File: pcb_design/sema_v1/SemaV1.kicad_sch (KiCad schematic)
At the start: 8 parts, among them IC1 PIC24FJ64GA002-I_SP

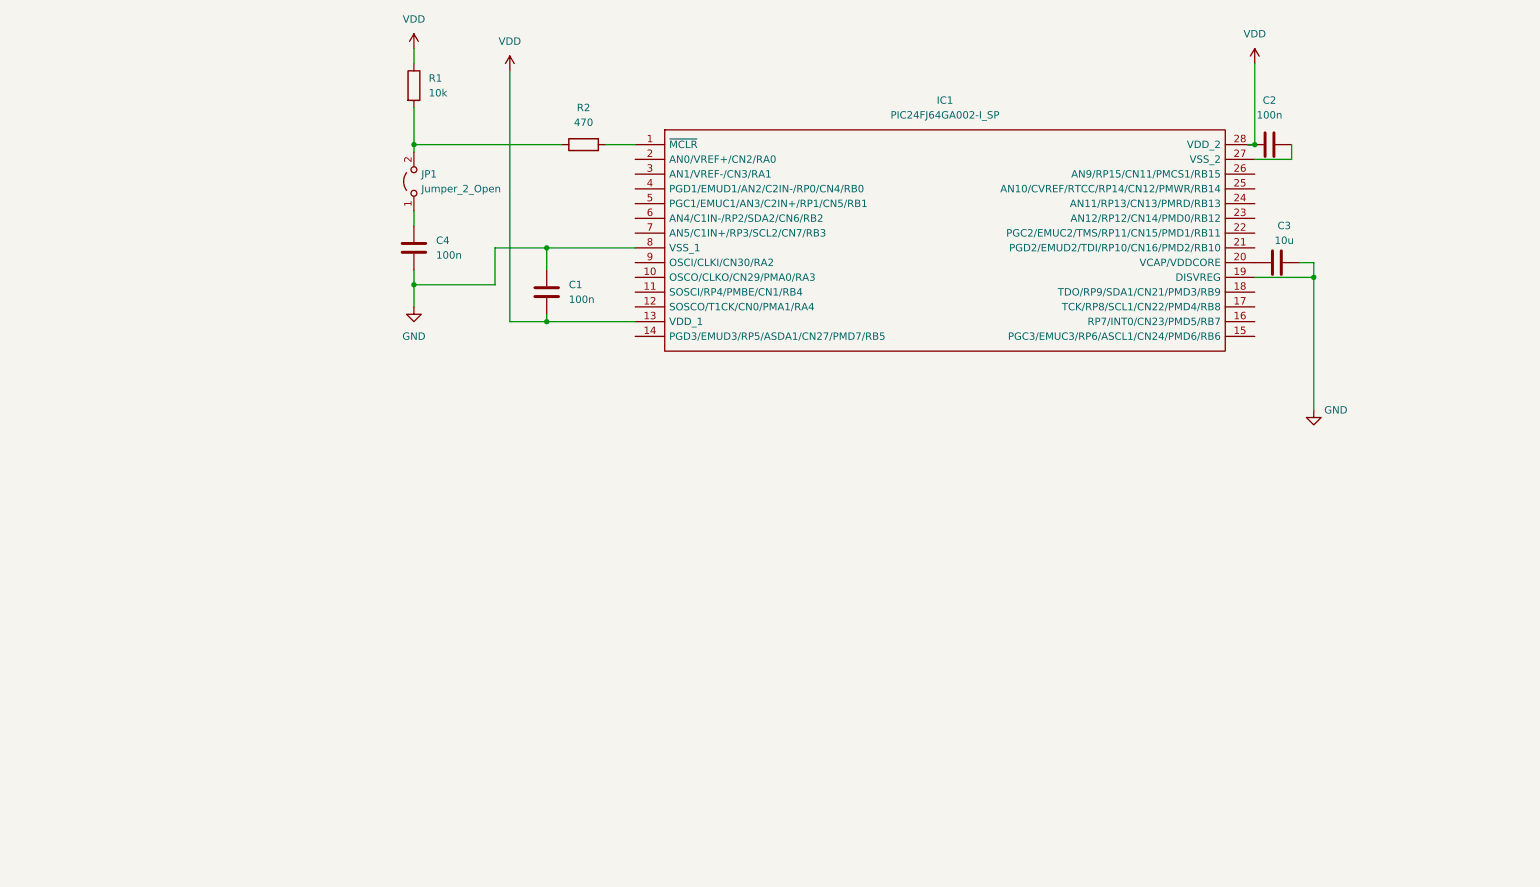
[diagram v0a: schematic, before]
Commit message: - Azuriranje seme
- Dodavanje modula za WiFi
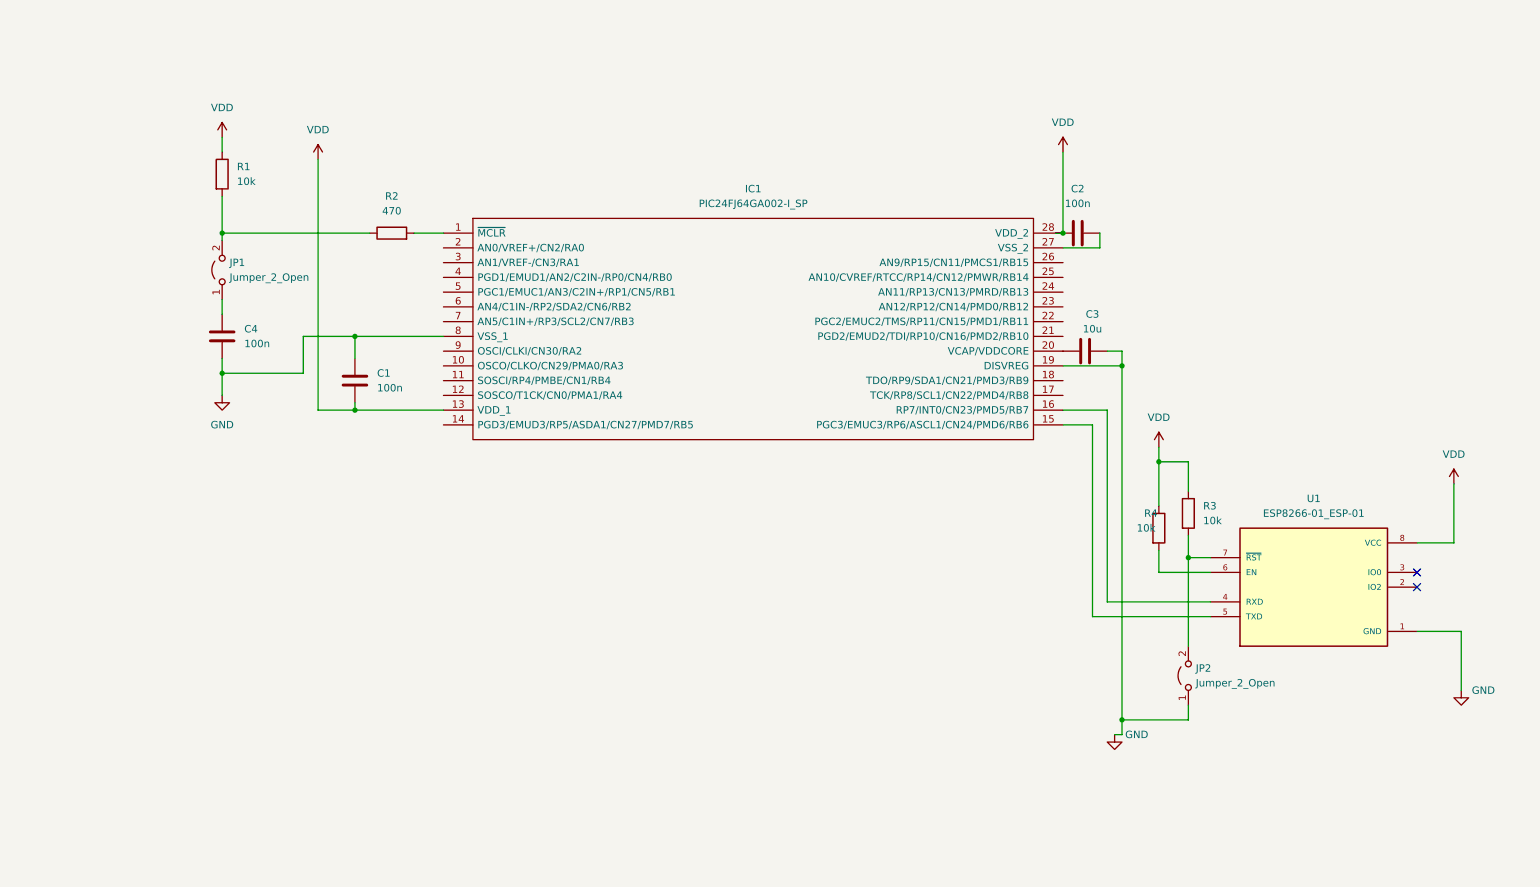
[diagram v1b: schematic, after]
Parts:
- added JP2: Jumper_2_Open, symbol Jumper:Jumper_2_Open
- added R3, R4: 10k, symbol Device:R
- added U1: ESP8266-01_ESP-01, ESP8266-01_ESP-01:XCVR_ESP8266-01_ESP-01, symbol ESP8266-01_ESP-01:ESP8266-01_ESP-01
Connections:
- net GND: now also JP2.1 (A), U1.1 (GND)
- net VDD: now also R3.1, R4.1, U1.8 (VCC)
- net at IC1.15 (PGC3/EMUC3/RP6/ASCL1/CN24/PMD6/RB6): now also U1.5 (TXD)
- net at IC1.16 (RP7/INT0/CN23/PMD5/RB7): now also U1.4 (RXD)
- new net: R4.2, U1.6 (EN)
- new net: JP2.2 (B), R3.2, U1.7 (~{RST})
- no-connect marks 0 -> 2
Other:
- moved on the sheet: C1, C2, C3, C4, IC1, JP1, R1, R2

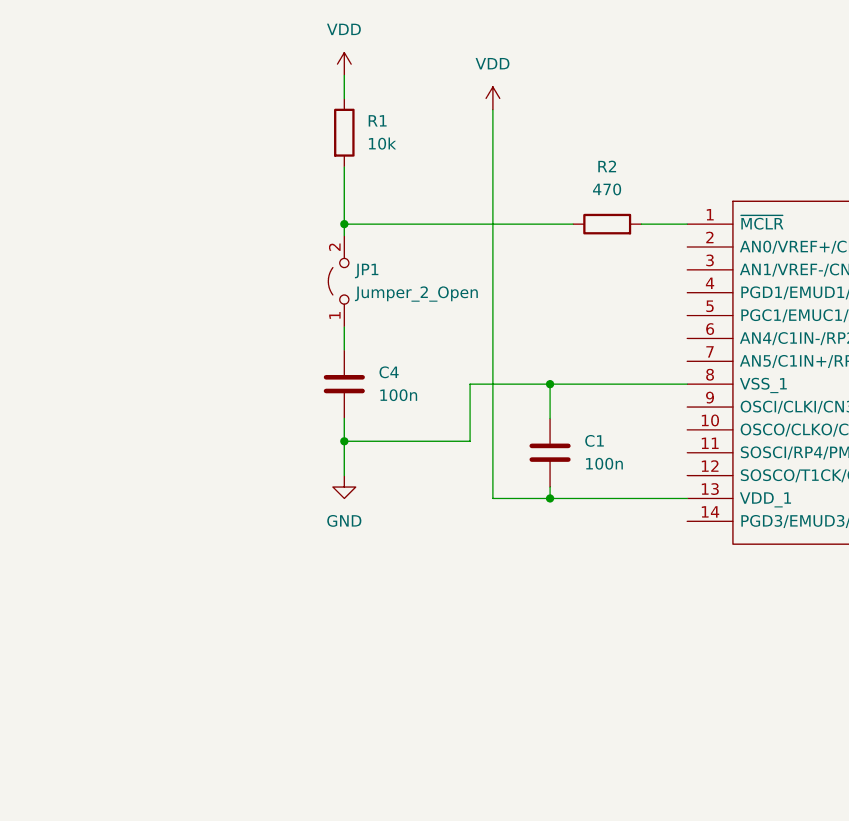
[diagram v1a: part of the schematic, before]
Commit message: -Dodavanje bloka za programiranje na šemu
  - Podrazumijeva dodavanje konektora za pinove i spajanja sa mikrokontrolerom
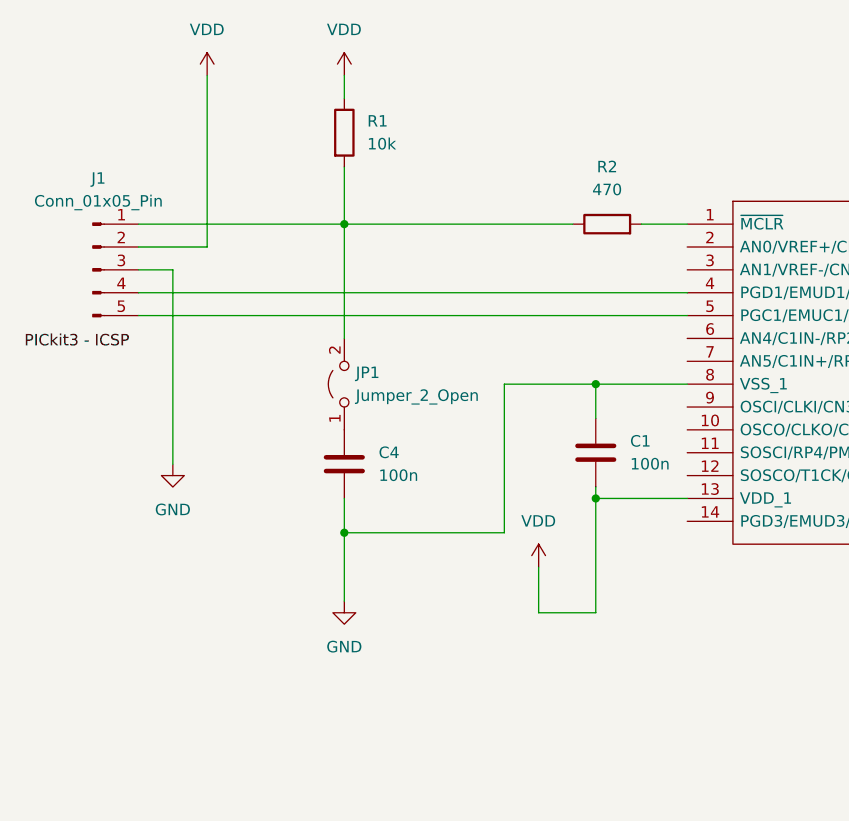
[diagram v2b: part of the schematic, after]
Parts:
- added J1: Conn_01x05_Pin, symbol Connector:Conn_01x05_Pin
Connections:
- net GND: now also J1.3 (Pin_3)
- net VDD: now also J1.2 (Pin_2)
- net at JP1.2 (B), R1.2, R2.1: now also J1.1 (Pin_1)
- net at IC1.4 (PGD1/EMUD1/AN2/C2IN-/RP0/CN4/RB0): now also J1.4 (Pin_4)
- net at IC1.5 (PGC1/EMUC1/AN3/C2IN+/RP1/CN5/RB1): now also J1.5 (Pin_5)
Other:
- moved on the sheet: C1, C4, JP1

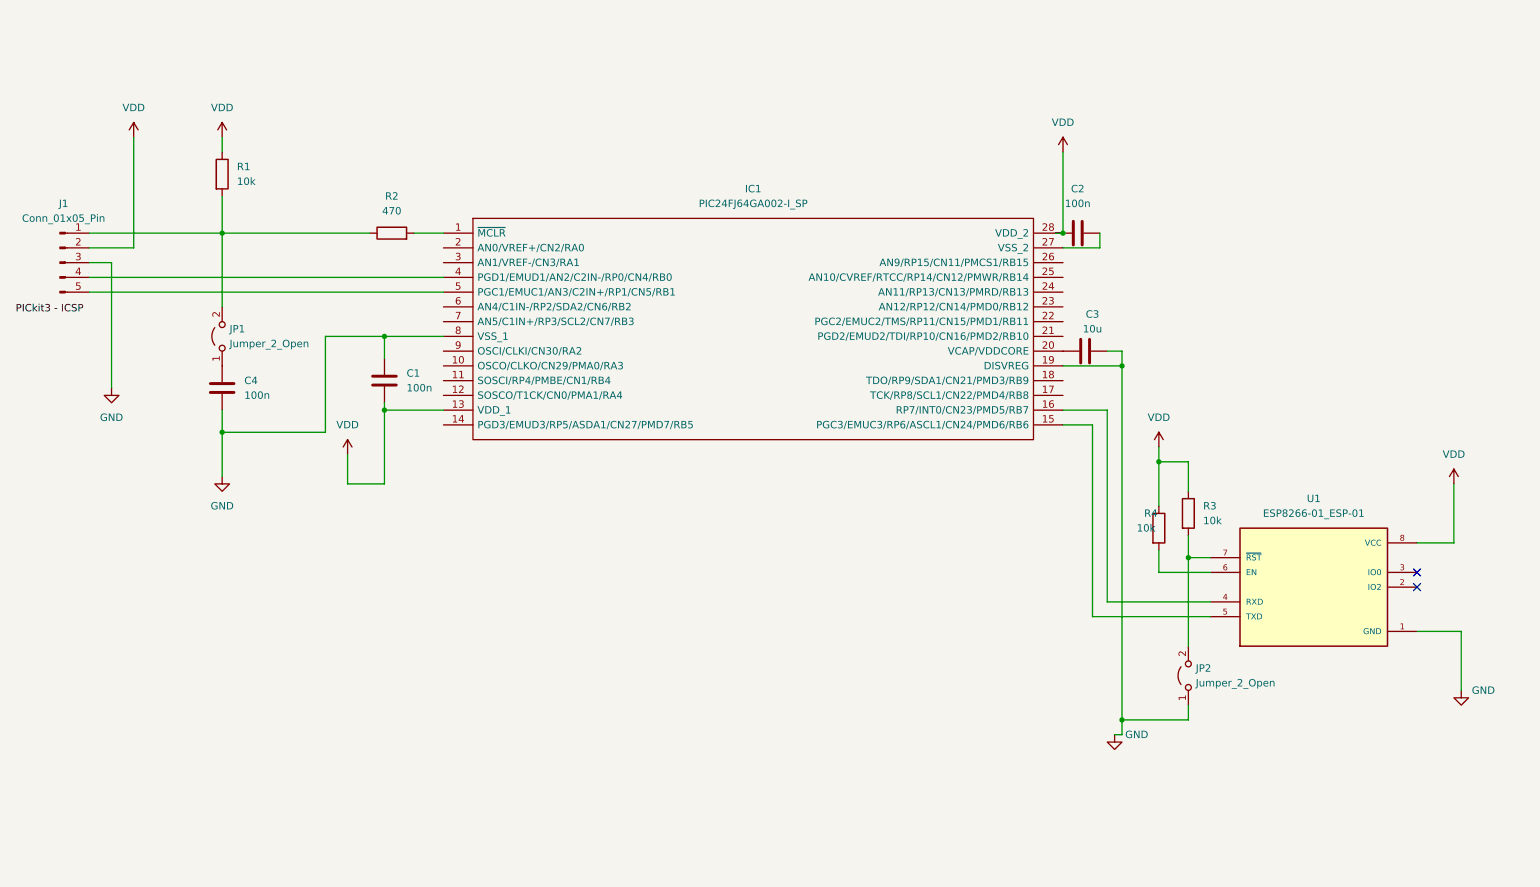
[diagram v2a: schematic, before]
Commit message: Azuriranje seme
 - Dodavanje edge connector-a na semu, spajanje I2C pinova sa mikrokontrolera i spajanje napajanja i mase

 - Dodavanje ostalih konektora za eksterne interfejse (I2C, UART, SPI)
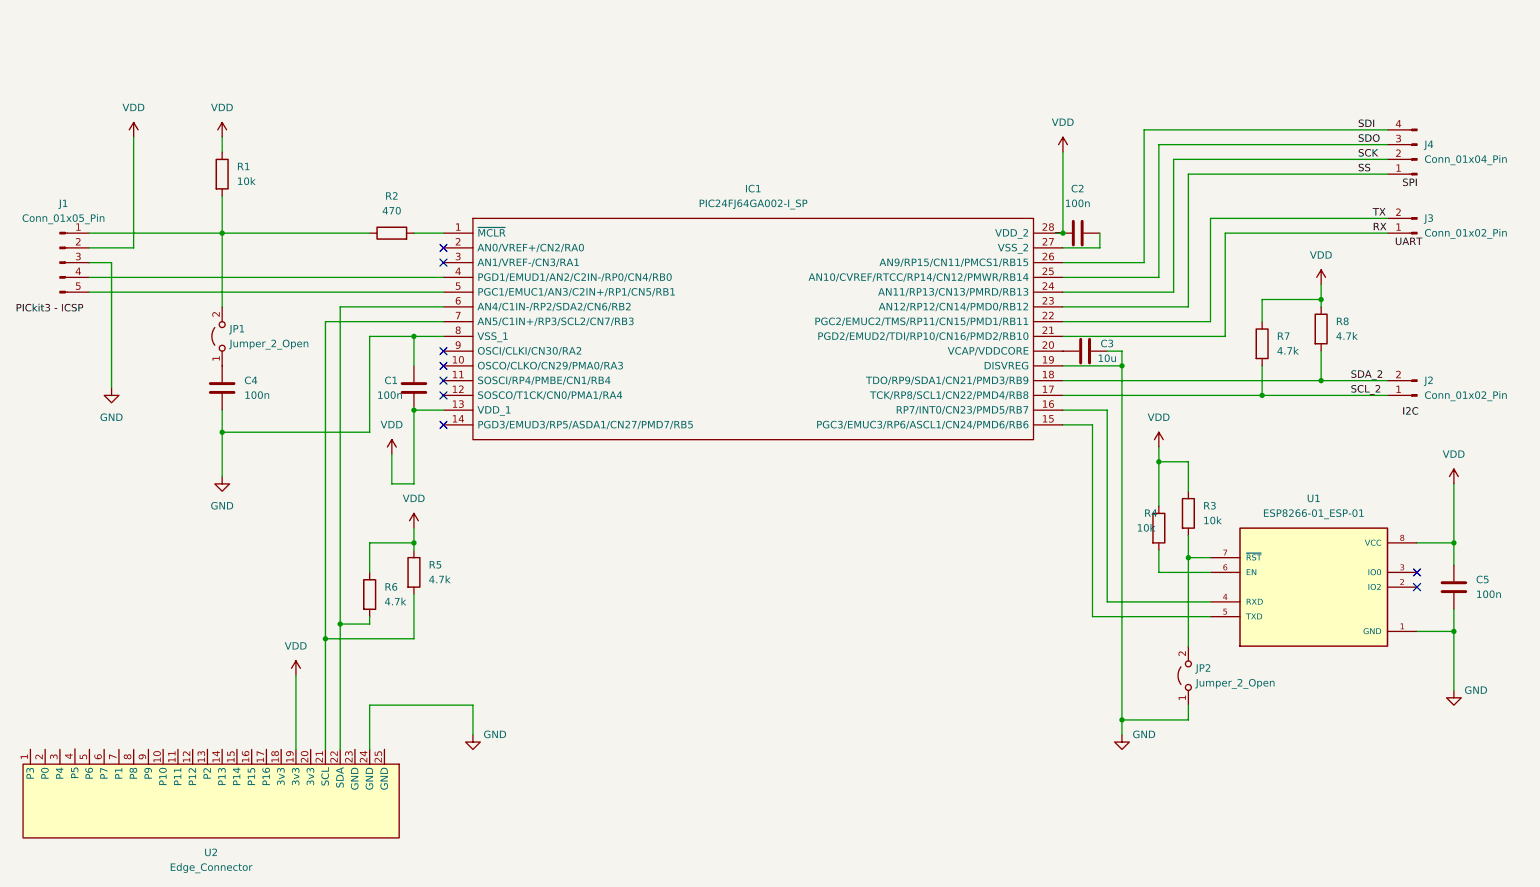
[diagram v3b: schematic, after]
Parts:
- added C5: 100n, symbol Device:C
- added J2, J3: Conn_01x02_Pin, symbol Connector:Conn_01x02_Pin
- added J4: Conn_01x04_Pin, symbol Connector:Conn_01x04_Pin
- added R5, R6, R7, R8: 4.7k, symbol Device:R
- added U2: ~, symbol Edge_Connector:Edge_Connector
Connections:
- net GND: now also C5.1, U2.24 (GND)
- net VDD: now also C5.2, R5.1, R6.1, R7.1, R8.1, U2.19 (3v3)
- net SCL_2: now reaches IC1.17 (TCK/RP8/SCL1/CN22/PMD4/RB8)
- net SCL_2: now also J2.1 (Pin_1), R7.2
- net SDA_2: now reaches IC1.18 (TDO/RP9/SDA1/CN21/PMD3/RB9)
- net SDA_2: now also J2.2 (Pin_2), R8.2
- net RX: now reaches IC1.21 (PGD2/EMUD2/TDI/RP10/CN16/PMD2/RB10)
- net RX: now also J3.1 (Pin_1)
- net TX: now reaches IC1.22 (PGC2/EMUC2/TMS/RP11/CN15/PMD1/RB11)
- net TX: now also J3.2 (Pin_2)
- net SS: now reaches IC1.23 (AN12/RP12/CN14/PMD0/RB12)
- net SS: now also J4.1 (Pin_1)
- net SCK: now reaches IC1.24 (AN11/RP13/CN13/PMRD/RB13)
- net SCK: now also J4.2 (Pin_2)
- net SDO: now reaches IC1.25 (AN10/CVREF/RTCC/RP14/CN12/PMWR/RB14)
- net SDO: now also J4.3 (Pin_3)
- net SDI: now reaches IC1.26 (AN9/RP15/CN11/PMCS1/RB15)
- net SDI: now also J4.4 (Pin_4)
- net at IC1.6 (AN4/C1IN-/RP2/SDA2/CN6/RB2): now also R6.2, U2.22 (SDA)
- net at IC1.7 (AN5/C1IN+/RP3/SCL2/CN7/RB3): now also R5.2, U2.21 (SCL)
- no-connect marks 2 -> 9
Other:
- moved on the sheet: C1
